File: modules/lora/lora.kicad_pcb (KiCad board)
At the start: 2 copper layers, 38.7 x 36.6 mm, 6 parts, among them U1 RFM95W-868S2

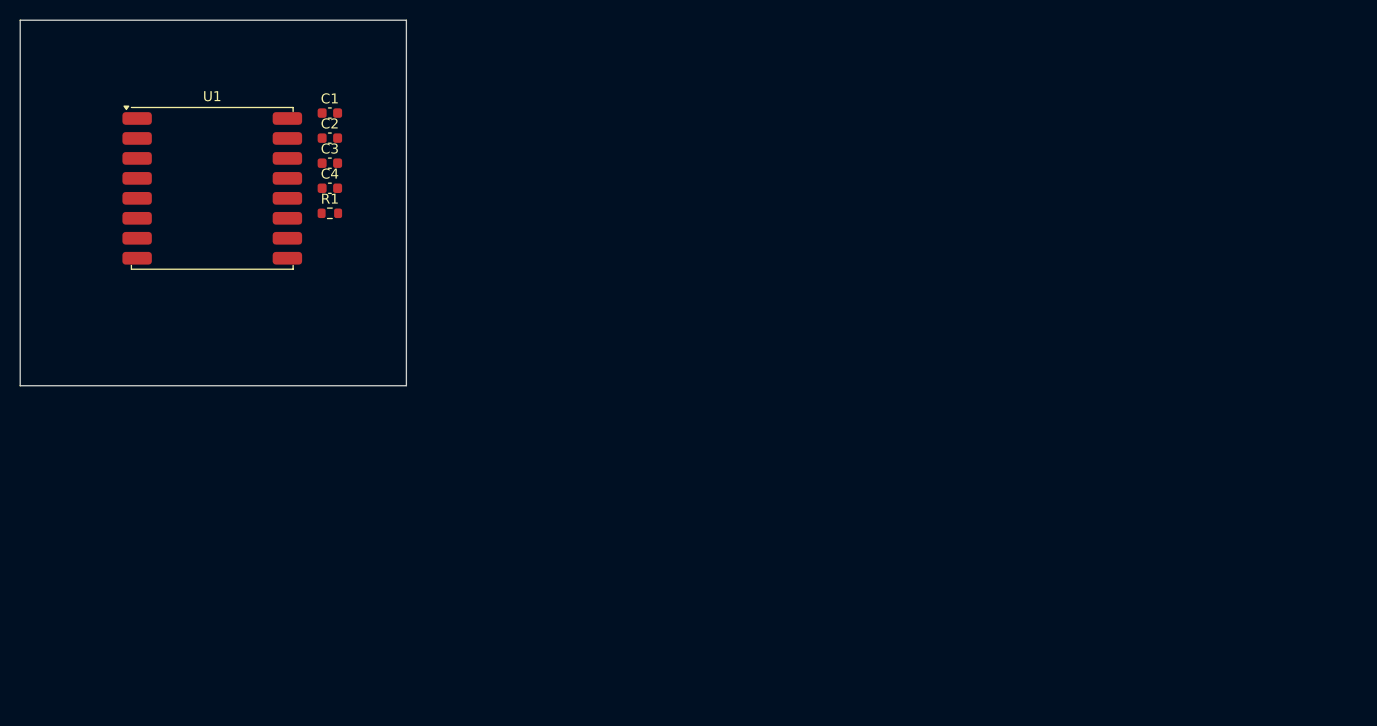
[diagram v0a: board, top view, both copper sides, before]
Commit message: Adding LoRa module
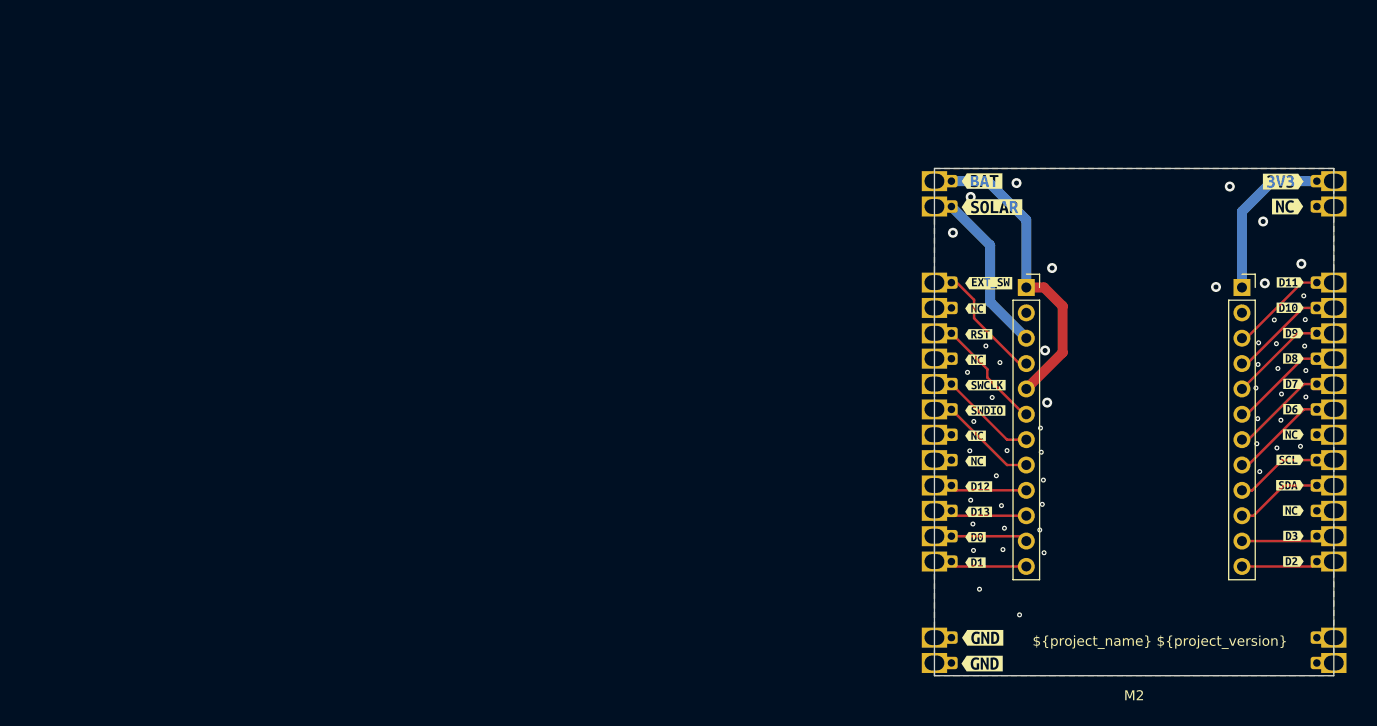
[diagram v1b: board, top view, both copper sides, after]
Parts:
- removed C1, C4: 10n, Capacitor_SMD:C_0603_1608Metric
- removed C2: 100n, Capacitor_SMD:C_0603_1608Metric
- removed C3: 2.2uF, Capacitor_SMD:C_0603_1608Metric
- removed R1: R0, Resistor_SMD:R_0603_1608Metric
- removed U1: RFM95W-868S2, RF_Module:HOPERF_RFM9XW_SMD
- added J1: LEFT, Connector_PinSocket_2.54mm:PinSocket_1x12_P2.54mm_Vertical, F.Cu at (170.5, 90.3)
- added J2: RIGHT, Connector_PinSocket_2.54mm:PinSocket_1x12_P2.54mm_Vertical, F.Cu at (192.1, 90.3)
- added M2: ~, MegaCastle:MegaCastle2x20-Module-I40.0x46.0-MBCFFF3CFFF3-SPAREPAD, F.Cu at (181.3, 103.8)
- added kibuzzard-69131742: G***, kibuzzard-69131742, F.Cu at (166.1, 79.7)
- added kibuzzard-69131759: G***, kibuzzard-69131759, F.Cu at (167.1, 82.3)
- added kibuzzard-6913178F1: G***, kibuzzard-6913178F, F.Cu at (166.8, 89.9)
- added kibuzzard-691317B6: G***, kibuzzard-691317B6, F.Cu at (166.2, 125.4)
- added kibuzzard-691317B6: G***, kibuzzard-691317B6, F.Cu at (166.1, 128.0)
- added kibuzzard-6913188E: G***, kibuzzard-6913188E, F.Cu at (165.4, 92.4)
- added kibuzzard-69131896: G***, kibuzzard-69131896, F.Cu at (165.8, 95.0)
- added kibuzzard-6913189D: G***, kibuzzard-6913189D, F.Cu at (165.4, 97.6)
- added kibuzzard-691318A4: G***, kibuzzard-691318A4, F.Cu at (166.4, 100.1)
- added kibuzzard-691318AC: G***, kibuzzard-691318AC, F.Cu at (166.4, 102.7)
- added kibuzzard-691318B3: G***, kibuzzard-691318B3, F.Cu at (165.4, 105.2)
- added kibuzzard-691318BA: G***, kibuzzard-691318BA, F.Cu at (165.4, 107.7)
- added kibuzzard-691318BF: G***, kibuzzard-691318BF, F.Cu at (165.8, 110.3)
- added kibuzzard-691318C6: G***, kibuzzard-691318C6, F.Cu at (165.8, 112.8)
- added kibuzzard-691318CD: G***, kibuzzard-691318CD, F.Cu at (165.4, 115.3)
- added kibuzzard-691318D3: G***, kibuzzard-691318D3, F.Cu at (165.4, 117.9)
- added kibuzzard-69131C88: G***, kibuzzard-69131C88, F.Cu at (197.0, 89.8)
- added kibuzzard-69131C8F: G***, kibuzzard-69131C8F, F.Cu at (197.0, 92.4)
- added kibuzzard-69131C99: G***, kibuzzard-69131C99, F.Cu at (197.3, 94.9)
- added kibuzzard-69131CA1: G***, kibuzzard-69131CA1, F.Cu at (197.3, 97.4)
- added kibuzzard-69131CAF: G***, kibuzzard-69131CAF, F.Cu at (197.3, 100.0)
- added kibuzzard-69131CB5: G***, kibuzzard-69131CB5, F.Cu at (197.3, 102.5)
- added kibuzzard-69131CBD: G***, kibuzzard-69131CBD, F.Cu at (197.3, 105.1)
- added kibuzzard-69131CC2: G***, kibuzzard-69131CC2, F.Cu at (196.9, 107.6)
- added kibuzzard-69131CC9: G***, kibuzzard-69131CC9, F.Cu at (196.9, 110.1)
- added kibuzzard-69131CCF: G***, kibuzzard-69131CCF, F.Cu at (197.3, 112.7)
- added kibuzzard-69131CD4: G***, kibuzzard-69131CD4, F.Cu at (197.3, 115.2)
- added kibuzzard-69131CD9: G***, kibuzzard-69131CD9, F.Cu at (197.3, 117.8)
- added kibuzzard-69131D58: G***, kibuzzard-69131D58, F.Cu at (196.7, 82.2)
- added kibuzzard-69131D76: G***, kibuzzard-69131D76, F.Cu at (196.3, 79.7)
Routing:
- net BAT: track 0.00 -> 30.1 mm
- net 3V3: track 0.00 -> 16.4 mm
- net SOLAR: track 0.00 -> 16.3 mm
- net EXT_SW: track 0.00 -> 11.9 mm
- net RST: track 0.00 -> 11.3 mm
- net SCL: track 0.00 -> 10.5 mm
- net D8: track 0.00 -> 9.81 mm
- net D10: track 0.00 -> 9.81 mm
- net SWDIO: track 0.00 -> 9.81 mm
- net SWCLK: track 0.00 -> 9.81 mm
- net D9: track 0.00 -> 9.81 mm
- net D7: track 0.00 -> 9.81 mm
- net D11: track 0.00 -> 9.81 mm
- net D6: track 0.00 -> 9.81 mm
- net SDA: track 0.00 -> 8.76 mm
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- added copper zone on B.Cu, net GND
- added copper zone on F.Cu, net GND
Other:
- board size 38.7 x 36.6 mm -> 40 x 50.8 mm
- board text added: "${project_name} ${project_version}"
